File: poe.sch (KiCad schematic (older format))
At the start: 31 parts, among them IC1 TPS2378DDA

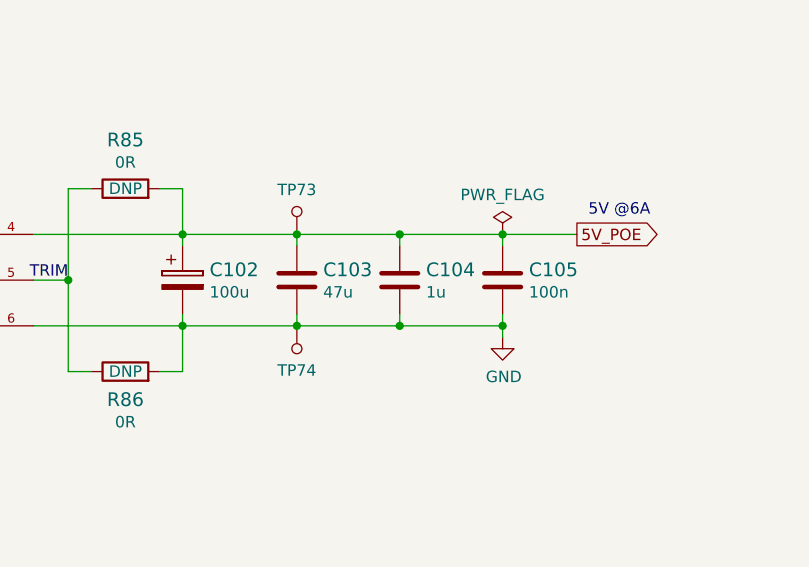
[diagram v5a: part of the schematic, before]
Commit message: Change C102 to ceramic, add one more capacitor
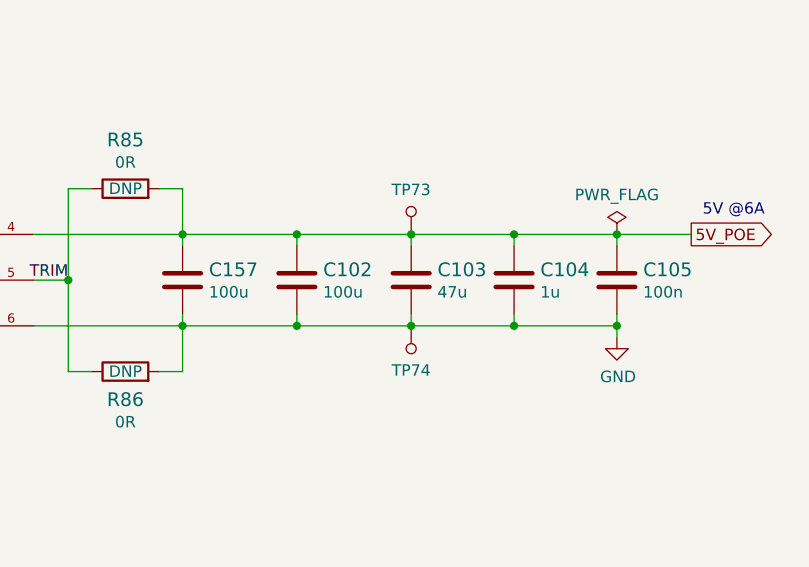
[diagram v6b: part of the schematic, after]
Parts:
- removed C102: C_100u_KEMET_A, sa800u-baseboard-hw-footprints:KEMET_A, symbol sa800u-baseboard-hw:C_100u_KEMET_A
- added C102, C157: C_100u_0805, sa800u-baseboard-hw-footprints:0805-cap, symbol sa800u-baseboard-hw:C_100u_0805
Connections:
- net 5V_POE: now also C102.1, C157.1
- net GND: now also C102.2, C157.2
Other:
- moved on the sheet: C103, C104, C105, TP73, TP74
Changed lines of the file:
@@
 L sa800u-baseboard-hw:GND #PWR0153
 U 1 1 61A46067
-P 14025 5075
-F 0 "#PWR0153" H 14025 4825 50  0001 C CNN
-F 1 "GND" H 14030 4902 50  0000 C CNN
-F 2 "" H 14025 5075 50  0001 C CNN
-F 3 "" H 14025 5075 50  0001 C CNN
-	1    14025 5075
-	1    0    0    -1
-$EndComp
-Wire Wire Line
-	14025 4675 14025 4625
-Wire Wire Line
-	14025 4975 14025 5025
+P 14525 5075
+F 0 "#PWR0153" H 14525 4825 50  0001 C CNN
+F 1 "GND" H 14530 4902 50  0000 C CNN
+F 2 "" H 14525 5075 50  0001 C CNN
+F 3 "" H 14525 5075 50  0001 C CNN
+	1    14525 5075
+	1    0    0    -1
+$EndComp
+Wire Wire Line
+	14525 4675 14525 4625
+Wire Wire Line
+	14525 4975 14525 5025
 $Comp
 L sa800u-baseboard-hw:C_100n_0402 C105
 U 1 1 61A46078
-P 14025 4825
-F 0 "C105" H 14140 4870 60  0000 L CNN
-F 1 "C_100n_0402" H 14025 4675 60  0001 C CNN
-F 2 "sa800u-baseboard-hw-footprints:0402-cap" H 14225 5025 60  0001 L CNN
-F 3 "" H 14025 4825 50  0001 C CNN
-F 4 "Walsin" H 14225 5225 60  0001 L CNN "Manufacturer"
-F 5 "0402X104K6R3CT" H 14225 5125 60  0001 L CNN "MPN"
-F 6 "100n" H 14140 4772 50  0000 L CNN "Val"
-	1    14025 4825
-	1    0    0    -1
-$EndComp
-Wire Wire Line
-	13575 4675 13575 4625
-Wire Wire Line
-	13575 4975 13575 5025
+P 14525 4825
+F 0 "C105" H 14640 4870 60  0000 L CNN
+F 1 "C_100n_0402" H 14525 4675 60  0001 C CNN
+F 2 "sa800u-baseboard-hw-footprints:0402-cap" H 14725 5025 60  0001 L CNN
+F 3 "" H 14525 4825 50  0001 C CNN
+F 4 "Walsin" H 14725 5225 60  0001 L CNN "Manufacturer"
+F 5 "0402X104K6R3CT" H 14725 5125 60  0001 L CNN "MPN"
+F 6 "100n" H 14640 4772 50  0000 L CNN "Val"
+	1    14525 4825
+	1    0    0    -1
+$EndComp
+Wire Wire Line
+	14075 4675 14075 4625
+Wire Wire Line
+	14075 4975 14075 5025
 $Comp
 L sa800u-baseboard-hw:C_1u_0402 C104
 U 1 1 61A46087
-P 13575 4825
-F 0 "C104" H 13690 4870 60  0000 L CNN
-F 1 "C_1u_0402" H 13575 4675 60  0001 C CNN
-F 2 "sa800u-baseboard-hw-footprints:0402-cap" H 13775 5025 60  0001 L CNN
-F 3 "" H 13575 4825 50  0001 C CNN
-F 4 "TDK" H 13775 5225 60  0001 L CNN "Manufacturer"
-F 5 "C1005X6S1A105K050BC" H 13775 5125 60  0001 L CNN "MPN"
-F 6 "1u" H 13690 4772 50  0000 L CNN "Val"
-	1    13575 4825
-	1    0    0    -1
-$EndComp
-Wire Wire Line
-	13125 4975 13125 5025
-Wire Wire Line
-	13125 4625 13125 4675
+P 14075 4825
+F 0 "C104" H 14190 4870 60  0000 L CNN
+F 1 "C_1u_0402" H 14075 4675 60  0001 C CNN
+F 2 "sa800u-baseboard-hw-footprints:0402-cap" H 14275 5025 60  0001 L CNN
+F 3 "" H 14075 4825 50  0001 C CNN
+F 4 "TDK" H 14275 5225 60  0001 L CNN "Manufacturer"
+F 5 "C1005X6S1A105K050BC" H 14275 5125 60  0001 L CNN "MPN"
+F 6 "1u" H 14190 4772 50  0000 L CNN "Val"
+	1    14075 4825
+	1    0    0    -1
+$EndComp
+Wire Wire Line
+	13625 4975 13625 5025
+Wire Wire Line
+	13625 4625 13625 4675
 $Comp
 L sa800u-baseboard-hw:C_47u_0805 C103
 U 1 1 61A46095
-P 13125 4825
-F 0 "C103" H 13240 4870 60  0000 L CNN
-F 1 "C_47u_0805" H 13125 4675 60  0001 C CNN
-F 2 "sa800u-baseboard-hw-footprints:0805-cap" H 13325 5025 60  0001 L CNN
-F 3 "" H 13125 4825 50  0001 C CNN
-F 4 "KEMET" H 13325 5225 60  0001 L CNN "Manufacturer"
-F 5 "C0805C476M9PACTU" H 13325 5125 60  0001 L CNN "MPN"
-F 6 "47u" H 13240 4772 50  0000 L CNN "Val"
-	1    13125 4825
+P 13625 4825
+F 0 "C103" H 13740 4870 60  0000 L CNN
+F 1 "C_47u_0805" H 13625 4675 60  0001 C CNN
+F 2 "sa800u-baseboard-hw-footprints:0805-cap" H 13825 5025 60  0001 L CNN
+F 3 "" H 13625 4825 50  0001 C CNN
+F 4 "KEMET" H 13825 5225 60  0001 L CNN "Manufacturer"
+F 5 "C0805C476M9PACTU" H 13825 5125 60  0001 L CNN "MPN"
+F 6 "47u" H 13740 4772 50  0000 L CNN "Val"
+	1    13625 4825
 	1    0    0    -1
 $EndComp
@@
 Wire Wire Line
 	12625 4625 12625 4675
-$Comp
-L sa800u-baseboard-hw:C_100u_KEMET_A C102
-U 1 1 61A460A3
-P 12625 4775
-F 0 "C102" H 12743 4770 60  0000 L CNN
-F 1 "C_100u_KEMET_A" H 12625 4625 60  0001 C CNN
-F 2 "sa800u-baseboard-hw-footprints:KEMET_A" H 12825 4975 60  0001 L CNN
-F 3 "" H 12625 4775 50  0001 C CNN
-F 4 "VISHAY" H 12825 5175 60  0001 L CNN "Manufacturer"
-F 5 "298D107X06R3A2T" H 12825 5075 60  0001 L CNN "MPN"
-F 6 "100u" H 12743 4672 50  0000 L CNN "Val"
-	1    12625 4775
-	1    0    0    -1
-$EndComp
-Wire Wire Line
-	14025 5025 14025 5075
+Wire Wire Line
+	14525 5025 14525 5075
 Wire Wire Line
 	12125 4825 11975 4825
@@
 Text Label 6800 5475 0    50   ~ 0
 RTN
-Text GLabel 14350 4625 2    50   Output ~ 0
+Text GLabel 14850 4625 2    50   Output ~ 0
 5V_POE
-Text Notes 14400 4550 0    50   ~ 0
+Text Notes 14900 4550 0    50   ~ 0
 5V @6A
 $Comp
 L sa800u-baseboard-hw:PWR_FLAG #FLG?
 U 1 1 6640FF6B
-P 14025 4625
+P 14525 4625
 AR Path="/61B0DC30/6640FF6B" Ref="#FLG?"  Part="1"
 AR Path="/61DC2BE0/6640FF6B" Ref="#FLG?"  Part="1"
 AR Path="/61A19323/6640FF6B" Ref="#FLG0117"  Part="1"
-F 0 "#FLG0117" H 14025 4700 50  0001 C CNN
-F 1 "PWR_FLAG" H 14025 4798 50  0000 C CNN
-F 2 "" H 14025 4625 50  0001 C CNN
-F 3 "~" H 14025 4625 50  0001 C CNN
-	1    14025 4625
-	1    0    0    -1
-$EndComp
-Connection ~ 14025 4625
-Wire Wire Line
-	14025 4625 14350 4625
-Connection ~ 13125 4625
-Connection ~ 13575 4625
-Wire Wire Line
-	12625 4625 13125 4625
-Wire Wire Line
-	12625 5025 13125 5025
-Wire Wire Line
-	13125 4625 13575 4625
-Connection ~ 14025 5025
-Wire Wire Line
-	13575 4625 14025 4625
-Wire Wire Line
-	13575 5025 14025 5025
-Wire Wire Line
-	13575 5025 13125 5025
-Connection ~ 13575 5025
-Connection ~ 13125 5025
+F 0 "#FLG0117" H 14525 4700 50  0001 C CNN
+F 1 "PWR_FLAG" H 14525 4798 50  0000 C CNN
+F 2 "" H 14525 4625 50  0001 C CNN
+F 3 "~" H 14525 4625 50  0001 C CNN
+	1    14525 4625
+	1    0    0    -1
+$EndComp
+Connection ~ 14525 4625
+Wire Wire Line
+	14525 4625 14850 4625
+Connection ~ 13625 4625
+Connection ~ 14075 4625
+Wire Wire Line
+	13125 5025 13625 5025
+Wire Wire Line
+	13625 4625 14075 4625
+Connection ~ 14525 5025
+Wire Wire Line
+	14075 4625 14525 4625
+Wire Wire Line
+	14075 5025 14525 5025
+Wire Wire Line
+	14075 5025 13625 5025
+Connection ~ 14075 5025
+Connection ~ 13625 5025
 Connection ~ 10550 4625
 Wire Wire Line
@@
 L sa800u-baseboard-hw:TP_SMD1MM TP73
 U 1 1 62413367
-P 13125 4525
-F 0 "TP73" H 13125 4430 50  0000 C CNN
-F 1 "TP_SMD1MM" H 13125 4425 50  0001 C CNN
-F 2 "sa800u-baseboard-hw-footprints:Testpoint_smd_1mm" H 13325 4725 60  0001 L CNN
-F 3 "" H 13325 4825 60  0001 L CNN
-	1    13125 4525
+P 13625 4525
+F 0 "TP73" H 13625 4430 50  0000 C CNN
+F 1 "TP_SMD1MM" H 13625 4425 50  0001 C CNN
+F 2 "sa800u-baseboard-hw-footprints:Testpoint_smd_1mm" H 13825 4725 60  0001 L CNN
+F 3 "" H 13825 4825 60  0001 L CNN
+	1    13625 4525
 	-1   0    0    1
 $EndComp
@@
 L sa800u-baseboard-hw:TP_SMD1MM TP74
 U 1 1 62416240
-P 13125 5125
-F 0 "TP74" H 13125 5030 50  0000 C CNN
-F 1 "TP_SMD1MM" H 13125 5025 50  0001 C CNN
-F 2 "sa800u-baseboard-hw-footprints:Testpoint_smd_1mm" H 13325 5325 60  0001 L CNN
-F 3 "" H 13325 5425 60  0001 L CNN
-	1    13125 5125
+P 13625 5125
+F 0 "TP74" H 13625 5030 50  0000 C CNN
+F 1 "TP_SMD1MM" H 13625 5025 50  0001 C CNN
+F 2 "sa800u-baseboard-hw-footprints:Testpoint_smd_1mm" H 13825 5325 60  0001 L CNN
+F 3 "" H 13825 5425 60  0001 L CNN
+	1    13625 5125
 	1    0    0    -1
 $EndComp
@@
 Text Notes 8475 5825 0    50   ~ 0
 ~~10mA need to be drawn from PSE to maintain PoE.\nPDQE30-D draws 8~~15mA with no load\nThis circuit provides exrta ~~3mA and indicates VDD presence
+$Comp
+L sa800u-baseboard-hw:C_100u_0805 C?
+U 1 1 67766E94
+P 13125 4825
+AR Path="/61A4BC4F/67766E94" Ref="C?"  Part="1"
+AR Path="/61A19323/67766E94" Ref="C102"  Part="1"
+F 0 "C102" H 13240 4870 60  0000 L CNN
+F 1 "C_100u_0805" H 13125 4675 60  0001 C CNN
+F 2 "sa800u-baseboard-hw-footprints:0805-cap" H 13325 5025 60  0001 L CNN
+F 3 "" H 13125 4825 50  0001 C CNN
+F 4 "MURATA" H 13325 5225 60  0001 L CNN "Manufacturer"
+F 5 "GRM21BR60J107ME15L" H 13325 5125 60  0001 L CNN "MPN"
+F 6 "100u" H 13240 4772 50  0000 L CNN "Val"
+	1    13125 4825
+	1    0    0    -1
+$EndComp
+Wire Wire Line
+	12625 4625 13125 4625
+Wire Wire Line
+	13125 4625 13125 4675
+Connection ~ 13125 4625
+Wire Wire Line
+	13125 4625 13625 4625
+Wire Wire Line
+	13125 4975 13125 5025
+Wire Wire Line
+	13125 5025 12625 5025
+Connection ~ 13125 5025
+$Comp
+L sa800u-baseboard-hw:C_100u_0805 C?
+U 1 1 677ADC2D
+P 12625 4825
+AR Path="/61A4BC4F/677ADC2D" Ref="C?"  Part="1"
+AR Path="/61A19323/677ADC2D" Ref="C157"  Part="1"
+F 0 "C157" H 12740 4870 60  0000 L CNN
+F 1 "C_100u_0805" H 12625 4675 60  0001 C CNN
+F 2 "sa800u-baseboard-hw-footprints:0805-cap" H 12825 5025 60  0001 L CNN
+F 3 "" H 12625 4825 50  0001 C CNN
+F 4 "MURATA" H 12825 5225 60  0001 L CNN "Manufacturer"
+F 5 "GRM21BR60J107ME15L" H 12825 5125 60  0001 L CNN "MPN"
+F 6 "100u" H 12740 4772 50  0000 L CNN "Val"
+	1    12625 4825
+	1    0    0    -1
+$EndComp
 $EndSCHEMATC

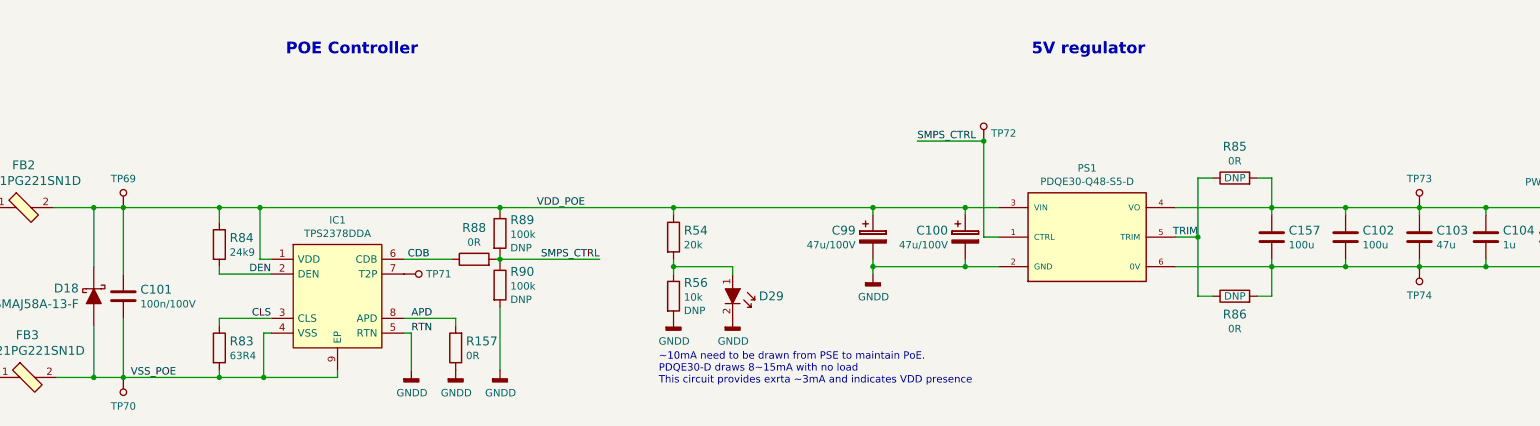
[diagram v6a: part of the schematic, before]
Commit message: Add testpoints to PCB, udpate cache, connect STUSB4500 reset to SoM and pulldown with 10k
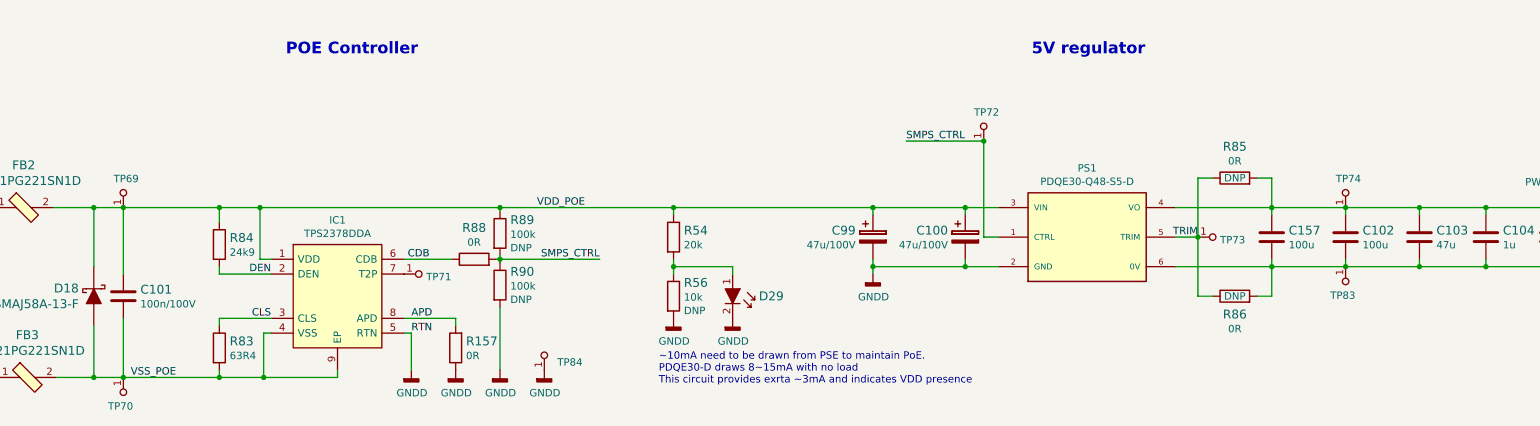
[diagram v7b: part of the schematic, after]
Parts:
- removed TP69, TP70, TP71, TP72, TP73, TP74: TP_SMD1MM, sa800u-baseboard-hw-footprints:Testpoint_smd_1mm, symbol sa800u-baseboard-hw:TP_SMD1MM
- added TP69, TP70, TP71, TP72, TP73, TP74, TP83, TP84: TP, antmicro-footprints:TP-R-1.5, symbol antmicroTestPoints:TP
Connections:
- net 5V_POE: now also TP74.1
- net GND: now also TP83.1
- net GNDD: now also TP84.1
- net SMPS_CTRL: now also TP72.1
- net TRIM: now also TP73.1
- net VDD_POE: now also TP69.1
- net VSS_POE: now also TP70.1
- net at IC1.7 (T2P): now also TP71.1
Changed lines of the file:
@@
 Wire Wire Line
 	10675 4825 10675 4175
-Text Label 10225 4175 0    50   ~ 0
+Text Label 10150 4175 0    50   ~ 0
 SMPS_CTRL
 Connection ~ 10550 5025
@@
 Wire Wire Line
 	8575 4625 9925 4625
-$Comp
-L sa800u-baseboard-hw:TP_SMD1MM TP69
-U 1 1 62405733
-P 4850 4525
-F 0 "TP69" H 4850 4430 50  0000 C CNN
-F 1 "TP_SMD1MM" H 4850 4425 50  0001 C CNN
-F 2 "sa800u-baseboard-hw-footprints:Testpoint_smd_1mm" H 5050 4725 60  0001 L CNN
-F 3 "" H 5050 4825 60  0001 L CNN
-	1    4850 4525
-	-1   0    0    1
-$EndComp
-$Comp
-L sa800u-baseboard-hw:TP_SMD1MM TP72
-U 1 1 624090F9
-P 10675 4075
-F 0 "TP72" H 10625 4122 50  0000 R CNN
-F 1 "TP_SMD1MM" H 10675 3975 50  0001 C CNN
-F 2 "sa800u-baseboard-hw-footprints:Testpoint_smd_1mm" H 10875 4275 60  0001 L CNN
-F 3 "" H 10875 4375 60  0001 L CNN
-	1    10675 4075
-	-1   0    0    1
-$EndComp
-Wire Wire Line
-	10225 4175 10675 4175
-Connection ~ 10675 4175
-$Comp
-L sa800u-baseboard-hw:TP_SMD1MM TP73
-U 1 1 62413367
-P 13625 4525
-F 0 "TP73" H 13625 4430 50  0000 C CNN
-F 1 "TP_SMD1MM" H 13625 4425 50  0001 C CNN
-F 2 "sa800u-baseboard-hw-footprints:Testpoint_smd_1mm" H 13825 4725 60  0001 L CNN
-F 3 "" H 13825 4825 60  0001 L CNN
-	1    13625 4525
-	-1   0    0    1
-$EndComp
-$Comp
-L sa800u-baseboard-hw:TP_SMD1MM TP74
-U 1 1 62416240
-P 13625 5125
-F 0 "TP74" H 13625 5030 50  0000 C CNN
-F 1 "TP_SMD1MM" H 13625 5025 50  0001 C CNN
-F 2 "sa800u-baseboard-hw-footprints:Testpoint_smd_1mm" H 13825 5325 60  0001 L CNN
-F 3 "" H 13825 5425 60  0001 L CNN
-	1    13625 5125
-	1    0    0    -1
-$EndComp
-$Comp
-L sa800u-baseboard-hw:TP_SMD1MM TP70
-U 1 1 62420B0C
-P 4850 5875
-F 0 "TP70" H 4850 5780 50  0000 C CNN
-F 1 "TP_SMD1MM" H 4850 5775 50  0001 C CNN
-F 2 "sa800u-baseboard-hw-footprints:Testpoint_smd_1mm" H 5050 6075 60  0001 L CNN
-F 3 "" H 5050 6175 60  0001 L CNN
-	1    4850 5875
-	1    0    0    -1
-$EndComp
-$Comp
-L sa800u-baseboard-hw:TP_SMD1MM TP71
-U 1 1 624298A6
-P 6850 5075
-F 0 "TP71" V 6850 5025 50  0000 R CNN
-F 1 "TP_SMD1MM" H 6850 4975 50  0001 C CNN
-F 2 "sa800u-baseboard-hw-footprints:Testpoint_smd_1mm" H 7050 5275 60  0001 L CNN
-F 3 "" H 7050 5375 60  0001 L CNN
-	1    6850 5075
-	0    -1   -1   0
-$EndComp
+Wire Wire Line
+	10150 4175 10675 4175
 Text Notes 500  700  0    118  ~ 24
 PoE
@@
 	1    0    0    -1
 $EndComp
+$Comp
+L antmicroTestPoints:TP TP83
+U 1 1 68DA4045
+P 13125 5125
+F 0 "TP83" H 13106 5030 50  0000 C CNN
+F 1 "TP" H 13125 5125 50  0001 C CNN
+F 2 "antmicro-footprints:TP-R-1.5" H 13125 5125 50  0001 C CNN
+F 3 "" H 13125 5125 50  0001 C CNN
+	1    13125 5125
+	1    0    0    -1
+$EndComp
+$Comp
+L antmicroTestPoints:TP TP74
+U 1 1 68DAA5BD
+P 13125 4525
+F 0 "TP74" H 13106 4430 50  0000 C CNN
+F 1 "TP" H 13125 4525 50  0001 C CNN
+F 2 "antmicro-footprints:TP-R-1.5" H 13125 4525 50  0001 C CNN
+F 3 "" H 13125 4525 50  0001 C CNN
+	1    13125 4525
+	-1   0    0    1
+$EndComp
+$Comp
+L antmicroTestPoints:TP TP73
+U 1 1 68DB1530
+P 12225 4825
+F 0 "TP73" V 12206 4775 50  0000 R CNN
+F 1 "TP" H 12225 4825 50  0001 C CNN
+F 2 "antmicro-footprints:TP-R-1.5" H 12225 4825 50  0001 C CNN
+F 3 "" H 12225 4825 50  0001 C CNN
+	1    12225 4825
+	0    -1   -1   0
+$EndComp
+$Comp
+L antmicroTestPoints:TP TP72
+U 1 1 68DBC44F
+P 10675 4075
+F 0 "TP72" H 10656 3980 50  0000 C CNN
+F 1 "TP" H 10675 4075 50  0001 C CNN
+F 2 "antmicro-footprints:TP-R-1.5" H 10675 4075 50  0001 C CNN
+F 3 "" H 10675 4075 50  0001 C CNN
+	1    10675 4075
+	-1   0    0    1
+$EndComp
+Connection ~ 10675 4175
+$Comp
+L antmicroTestPoints:TP TP69
+U 1 1 68DC66B0
+P 4850 4525
+F 0 "TP69" H 4831 4430 50  0000 C CNN
+F 1 "TP" H 4850 4525 50  0001 C CNN
+F 2 "antmicro-footprints:TP-R-1.5" H 4850 4525 50  0001 C CNN
+F 3 "" H 4850 4525 50  0001 C CNN
+	1    4850 4525
+	-1   0    0    1
+$EndComp
+$Comp
+L antmicroTestPoints:TP TP70
+U 1 1 68DCEF78
+P 4850 5875
+F 0 "TP70" H 4831 5780 50  0000 C CNN
+F 1 "TP" H 4850 5875 50  0001 C CNN
+F 2 "antmicro-footprints:TP-R-1.5" H 4850 5875 50  0001 C CNN
+F 3 "" H 4850 5875 50  0001 C CNN
+	1    4850 5875
+	1    0    0    -1
+$EndComp
+$Comp
+L antmicroTestPoints:TP TP71
+U 1 1 68DD2B07
+P 6850 5075
+F 0 "TP71" V 6831 5025 50  0000 R CNN
+F 1 "TP" H 6850 5075 50  0001 C CNN
+F 2 "antmicro-footprints:TP-R-1.5" H 6850 5075 50  0001 C CNN
+F 3 "" H 6850 5075 50  0001 C CNN
+	1    6850 5075
+	0    -1   -1   0
+$EndComp
+$Comp
+L antmicroTestPoints:TP TP84
+U 1 1 68DDC004
+P 7700 5625
+F 0 "TP84" H 7612 5672 50  0000 R CNN
+F 1 "TP" H 7700 5625 50  0001 C CNN
+F 2 "antmicro-footprints:TP-R-1.5" H 7700 5625 50  0001 C CNN
+F 3 "" H 7700 5625 50  0001 C CNN
+	1    7700 5625
+	-1   0    0    1
+$EndComp
+$Comp
+L sa800u-baseboard-hw:GNDD #PWR0243
+U 1 1 68DDEE83
+P 7700 5725
+F 0 "#PWR0243" H 7700 5475 50  0001 C CNN
+F 1 "GNDD" H 7704 5570 50  0000 C CNN
+F 2 "" H 7700 5725 50  0001 C CNN
+F 3 "" H 7700 5725 50  0001 C CNN
+	1    7700 5725
+	1    0    0    -1
+$EndComp

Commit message: Clear annotation and annotate
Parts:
- renumbered C101 to C144, C99 to C145, C100 to C146, C157 to C147, C102 to C148, C103 to C149, C104 to C150, C105 to C151, D16 to D29, D17 to D30, D18 to D31, D29 to D32, FB2 to FB4, FB3 to FB5, IC1 to IC2, R84 to R143, R83 to R144, R157 to R145, R88 to R146, R89 to R147, R90 to R148, R54 to R149, R56 to R150, R85 to R151, R86 to R152, TP69 to TP78, TP70 to TP79, TP71 to TP80, TP84 to TP81, TP72 to TP82, TP73 to TP83, TP74 to TP84, TP83 to TP85
